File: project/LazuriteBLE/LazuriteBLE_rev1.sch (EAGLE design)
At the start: 21 parts

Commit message: update Lazurite BLE
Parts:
- added C16: 22u, rcl:C-EUC1206
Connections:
- net +5V: now also C16.1
- net BLE_CTS: now also U$1.P54; no longer U$1.P01
- net BLE_RX: now also U$1.P00; no longer U$1.P54
- net BLE_TX: now also U$1.P01; no longer U$1.P55
- net BLE_WAKEUP: now also U$1.P55; no longer U$1.P00
- net GND: now also C16.2
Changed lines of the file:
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@@
 <part name="+3V8" library="supply1" deviceset="+3V3" device=""/>
 <part name="+3V9" library="supply1" deviceset="+3V3" device=""/>
+<part name="GND19" library="supply1" deviceset="GND" device=""/>
+<part name="C16" library="rcl" deviceset="C-EU" device="C1206" value="22u"/>
 </parts>
 <sheets>
@@
 <instance part="+3V4" gate="G$1" x="220.98" y="215.9"/>
 <instance part="+3V5" gate="G$1" x="271.78" y="228.6"/>
-<instance part="P+3" gate="1" x="86.36" y="71.12"/>
+<instance part="P+3" gate="1" x="78.74" y="71.12"/>
 <instance part="+3V6" gate="G$1" x="132.08" y="73.66"/>
 <instance part="+3V7" gate="G$1" x="347.98" y="116.84"/>
 <instance part="+3V8" gate="G$1" x="27.94" y="198.12"/>
 <instance part="+3V9" gate="G$1" x="165.1" y="182.88"/>
+<instance part="GND19" gate="1" x="78.74" y="17.78"/>
+<instance part="C16" gate="G$1" x="78.74" y="30.48"/>
 </instances>
 <busses>
@@
 <junction x="231.14" y="200.66"/>
 </segment>
+<segment>
+<wire x1="78.74" y1="25.4" x2="78.74" y2="20.32" width="0.1524" layer="91"/>
+<pinref part="GND19" gate="1" pin="GND"/>
+<pinref part="C16" gate="G$1" pin="2"/>
+</segment>
 </net>
 <net name="P04" class="0">
@@
 <net name="BLE_RX" class="0">
 <segment>
-<wire x1="73.66" y1="205.74" x2="60.96" y2="205.74" width="0.1524" layer="91"/>
-<label x="58.42" y="205.74" size="1.778" layer="95"/>
-<pinref part="U$1" gate="G$1" pin="P54"/>
-</segment>
-<segment>
 <pinref part="U$4" gate="G$1" pin="21"/>
 <wire x1="261.62" y1="190.5" x2="269.24" y2="190.5" width="0.1524" layer="91"/>
 <label x="269.24" y="190.5" size="1.778" layer="95"/>
+</segment>
+<segment>
+<wire x1="132.08" y1="193.04" x2="144.78" y2="193.04" width="0.1524" layer="91"/>
+<label x="144.78" y="193.04" size="1.778" layer="95"/>
+<pinref part="U$1" gate="G$1" pin="P00"/>
 </segment>
 </net>
@@
 <net name="BLE_TX" class="0">
 <segment>
-<wire x1="73.66" y1="203.2" x2="60.96" y2="203.2" width="0.1524" layer="91"/>
-<label x="56.896" y="203.2" size="1.778" layer="95"/>
-<pinref part="U$1" gate="G$1" pin="P55"/>
-</segment>
-<segment>
 <pinref part="U$4" gate="G$1" pin="22"/>
 <wire x1="261.62" y1="187.96" x2="269.24" y2="187.96" width="0.1524" layer="91"/>
 <label x="269.24" y="187.96" size="1.778" layer="95"/>
+</segment>
+<segment>
+<wire x1="132.08" y1="195.58" x2="144.78" y2="195.58" width="0.1524" layer="91"/>
+<label x="144.78" y="195.58" size="1.778" layer="95"/>
+<pinref part="U$1" gate="G$1" pin="P01"/>
 </segment>
 </net>
@@
 </segment>
 <segment>
+<pinref part="C16" gate="G$1" pin="1"/>
+<pinref part="P+3" gate="1" pin="+5V"/>
+<wire x1="78.74" y1="68.58" x2="78.74" y2="58.42" width="0.1524" layer="91"/>
 <pinref part="U$6" gate="G$1" pin="STBY"/>
+<wire x1="78.74" y1="58.42" x2="78.74" y2="33.02" width="0.1524" layer="91"/>
 <wire x1="99.06" y1="58.42" x2="86.36" y2="58.42" width="0.1524" layer="91"/>
 <wire x1="86.36" y1="58.42" x2="86.36" y2="38.1" width="0.1524" layer="91"/>
@@
 <wire x1="86.36" y1="38.1" x2="86.36" y2="30.48" width="0.1524" layer="91"/>
 <pinref part="C14" gate="G$1" pin="1"/>
-<pinref part="P+3" gate="1" pin="+5V"/>
-<wire x1="86.36" y1="58.42" x2="86.36" y2="68.58" width="0.1524" layer="91"/>
+<wire x1="78.74" y1="58.42" x2="86.36" y2="58.42" width="0.1524" layer="91"/>
 <junction x="86.36" y="58.42"/>
+<junction x="78.74" y="58.42"/>
 </segment>
 </net>
@@
 </segment>
 <segment>
-<wire x1="132.08" y1="193.04" x2="144.78" y2="193.04" width="0.1524" layer="91"/>
-<label x="144.78" y="193.04" size="1.778" layer="95"/>
-<pinref part="U$1" gate="G$1" pin="P00"/>
+<wire x1="73.66" y1="203.2" x2="60.96" y2="203.2" width="0.1524" layer="91"/>
+<label x="56.896" y="203.2" size="1.778" layer="95"/>
+<pinref part="U$1" gate="G$1" pin="P55"/>
 </segment>
 </net>
@@
 </segment>
 <segment>
-<wire x1="132.08" y1="195.58" x2="144.78" y2="195.58" width="0.1524" layer="91"/>
-<label x="144.78" y="195.58" size="1.778" layer="95"/>
-<pinref part="U$1" gate="G$1" pin="P01"/>
-</segment>
-</net>
+<wire x1="73.66" y1="205.74" x2="60.96" y2="205.74" width="0.1524" layer="91"/>
+<label x="58.42" y="205.74" size="1.778" layer="95"/>
+<pinref part="U$1" gate="G$1" pin="P54"/>
+</segment>
+</net>

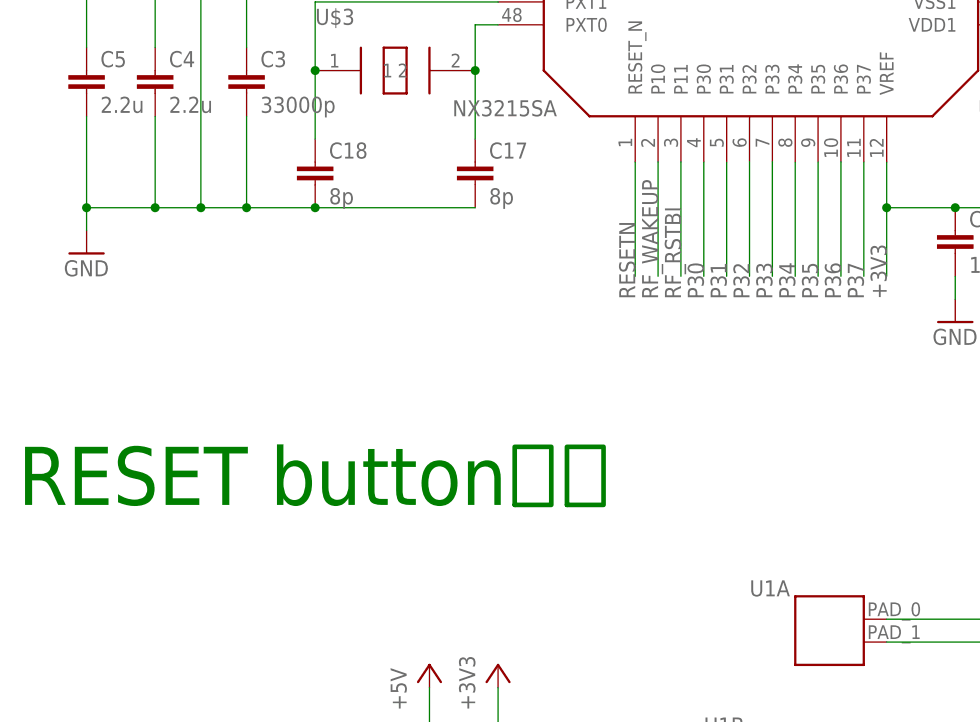
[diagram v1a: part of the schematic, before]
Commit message: updata Lazurite BLE and libraries of reset switch for LazuriteBLE.
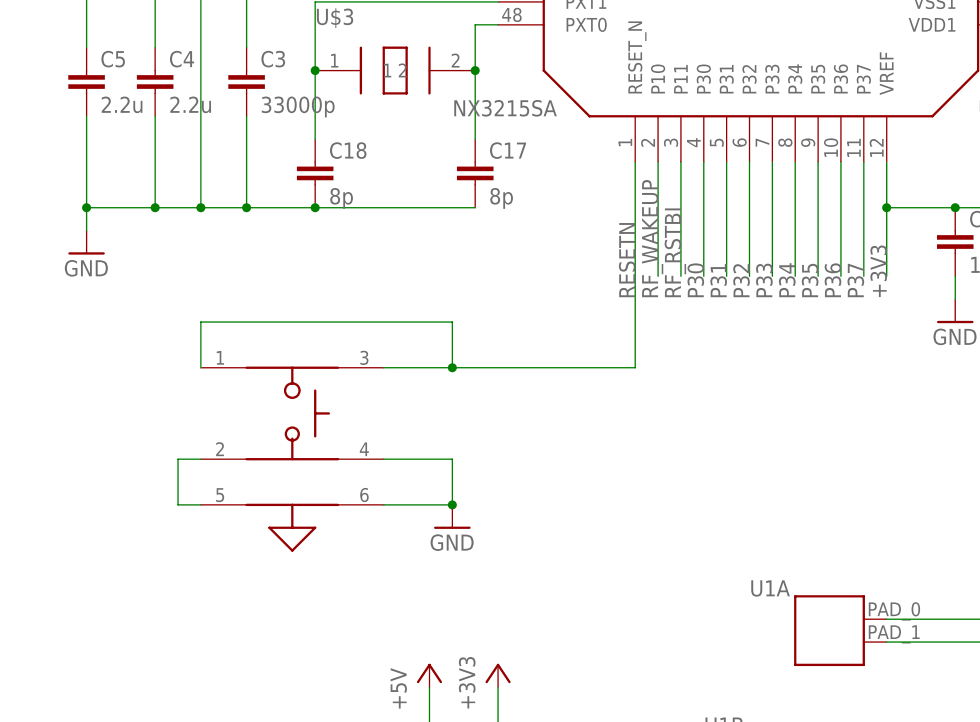
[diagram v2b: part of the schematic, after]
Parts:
- added SW1: SKSGACE010, lz-shield:SKSGACE010
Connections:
- new net N$11: SW1.2, SW1.5
- net GND: now also SW1.4, SW1.6
- net RESETN: now also SW1.1, SW1.3
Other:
- note removed: "RESET button追加"
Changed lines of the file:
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@@
 <part name="GND19" library="supply1" deviceset="GND" device=""/>
 <part name="C16" library="rcl" deviceset="C-EU" device="C1206" value="22u"/>
+<part name="SW1" library="lz-shield" deviceset="SKSGACE010" device=""/>
+<part name="GND12" library="supply1" deviceset="GND" device=""/>
 </parts>
 <sheets>
@@
 <text x="294.64" y="10.16" size="2.54" layer="91" font="vector">Naotaka Saito
 161229 preriminaly</text>
-<text x="20.32" y="124.46" size="6.4516" layer="91">RESET button追加</text>
 </plain>
 <instances>
@@
 <instance part="GND19" gate="1" x="78.74" y="17.78"/>
 <instance part="C16" gate="G$1" x="78.74" y="30.48"/>
+<instance part="SW1" gate="G$1" x="50.8" y="134.62"/>
+<instance part="GND12" gate="1" x="68.58" y="121.92"/>
 </instances>
 <busses>
@@
 <pinref part="C16" gate="G$1" pin="2"/>
 </segment>
+<segment>
+<pinref part="SW1" gate="G$1" pin="4"/>
+<wire x1="60.96" y1="129.54" x2="68.58" y2="129.54" width="0.1524" layer="91"/>
+<wire x1="68.58" y1="129.54" x2="68.58" y2="124.46" width="0.1524" layer="91"/>
+<pinref part="SW1" gate="G$1" pin="6"/>
+<wire x1="68.58" y1="124.46" x2="60.96" y2="124.46" width="0.1524" layer="91"/>
+<pinref part="GND12" gate="1" pin="GND"/>
+<junction x="68.58" y="124.46"/>
+</segment>
 </net>
 <net name="P04" class="0">
@@
 <net name="RESETN" class="0">
 <segment>
-<wire x1="88.9" y1="162.56" x2="88.9" y2="149.86" width="0.1524" layer="91"/>
+<wire x1="88.9" y1="162.56" x2="88.9" y2="139.7" width="0.1524" layer="91"/>
 <label x="88.9" y="147.32" size="1.778" layer="95" font="vector" rot="R90"/>
 <pinref part="U$1" gate="G$1" pin="RESET_N"/>
+<pinref part="SW1" gate="G$1" pin="1"/>
+<wire x1="40.64" y1="139.7" x2="40.64" y2="144.78" width="0.1524" layer="91"/>
+<wire x1="40.64" y1="144.78" x2="68.58" y2="144.78" width="0.1524" layer="91"/>
+<wire x1="68.58" y1="144.78" x2="68.58" y2="139.7" width="0.1524" layer="91"/>
+<pinref part="SW1" gate="G$1" pin="3"/>
+<wire x1="68.58" y1="139.7" x2="60.96" y2="139.7" width="0.1524" layer="91"/>
+<wire x1="88.9" y1="139.7" x2="68.58" y2="139.7" width="0.1524" layer="91"/>
+<junction x="68.58" y="139.7"/>
 </segment>
 </net>
@@
 </segment>
 </net>
+<net name="N$11" class="0">
+<segment>
+<pinref part="SW1" gate="G$1" pin="2"/>
+<wire x1="40.64" y1="129.54" x2="38.1" y2="129.54" width="0.1524" layer="91"/>
+<wire x1="38.1" y1="129.54" x2="38.1" y2="124.46" width="0.1524" layer="91"/>
+<pinref part="SW1" gate="G$1" pin="5"/>
+<wire x1="38.1" y1="124.46" x2="40.64" y2="124.46" width="0.1524" layer="91"/>
+</segment>
+</net>
